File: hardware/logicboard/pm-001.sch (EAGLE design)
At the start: 16 parts, among them K1 G5V1, T1 2SC1815

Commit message: FTDI.
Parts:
- added FTDI: (no value), pinhead:PINHD-1X6
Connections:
- new net N$12: FTDI.2, U$1.GND4
- new net N$13: FTDI.3, U$1.VCC1
- new net N$14: FTDI.4, U$1.RX1-1
- new net N$15: FTDI.5, U$1.TX0-1
- new net N$16: FTDI.6, U$1.DTR
- new net N$9: FTDI.1, U$1.GND3
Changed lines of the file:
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@@
 <setting verticaltext="up"/>
 </settings>
-<grid distance="0.1" unitdist="inch" unit="inch" style="dots" multiple="1" display="yes" altdistance="0.01" altunitdist="inch" altunit="inch"/>
+<grid distance="0.1" unitdist="inch" unit="inch" style="lines" multiple="1" display="no" altdistance="0.01" altunitdist="inch" altunit="inch"/>
 <layers>
 <layer number="1" name="Top" color="4" fill="1" visible="no" active="no"/>
@@
 <part name="FRONT" library="SparkFun-Connectors" library_urn="urn:adsk.eagle:library:513" deviceset="CONN_04" device="JST-PTH" package3d_urn="urn:adsk.eagle:package:38101/1"/>
 <part name="PWR12V" library="SparkFun-Connectors" deviceset="CONN_02" device="JST-PTH-2" value="12V"/>
+<part name="FTDI" library="pinhead" library_urn="urn:adsk.eagle:library:325" deviceset="PINHD-1X6" device="" package3d_urn="urn:adsk.eagle:package:22472/2"/>
 </parts>
 <sheets>
@@
 <instance part="FRONT" gate="G$1" x="5.08" y="76.2" rot="MR180"/>
 <instance part="PWR12V" gate="G$1" x="2.54" y="35.56" rot="MR180"/>
+<instance part="FTDI" gate="A" x="76.2" y="12.7" rot="R270"/>
 </instances>
 <busses>
@@
 </segment>
 </net>
+<net name="N$9" class="0">
+<segment>
+<pinref part="U$1" gate="G$1" pin="GND3"/>
+<pinref part="FTDI" gate="A" pin="1"/>
+<wire x1="83.82" y1="15.24" x2="83.82" y2="22.86" width="0.1524" layer="91"/>
+</segment>
+</net>
+<net name="N$12" class="0">
+<segment>
+<pinref part="U$1" gate="G$1" pin="GND4"/>
+<pinref part="FTDI" gate="A" pin="2"/>
+<wire x1="81.28" y1="15.24" x2="81.28" y2="22.86" width="0.1524" layer="91"/>
+</segment>
+</net>
+<net name="N$13" class="0">
+<segment>
+<pinref part="U$1" gate="G$1" pin="VCC1"/>
+<pinref part="FTDI" gate="A" pin="3"/>
+<wire x1="78.74" y1="15.24" x2="78.74" y2="22.86" width="0.1524" layer="91"/>
+</segment>
+</net>
+<net name="N$14" class="0">
+<segment>
+<pinref part="U$1" gate="G$1" pin="RX1-1"/>
+<pinref part="FTDI" gate="A" pin="4"/>
+<wire x1="76.2" y1="15.24" x2="76.2" y2="22.86" width="0.1524" layer="91"/>
+</segment>
+</net>
+<net name="N$15" class="0">
+<segment>
+<pinref part="U$1" gate="G$1" pin="TX0-1"/>
+<pinref part="FTDI" gate="A" pin="5"/>
+<wire x1="73.66" y1="15.24" x2="73.66" y2="22.86" width="0.1524" layer="91"/>
+</segment>
+</net>
+<net name="N$16" class="0">
+<segment>
+<pinref part="U$1" gate="G$1" pin="DTR"/>
+<pinref part="FTDI" gate="A" pin="6"/>
+<wire x1="71.12" y1="15.24" x2="71.12" y2="22.86" width="0.1524" layer="91"/>
+</segment>
+</net>

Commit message: D8 -> D2.
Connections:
- net N$7: now also U$1.D2; no longer U$1.D8
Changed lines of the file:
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@@
-</segment>
-</net>
-<net name="N$7" class="0">
-<segment>
-<pinref part="R2" gate="G$1" pin="1"/>
-<pinref part="U$1" gate="G$1" pin="D8"/>
-<wire x1="106.68" y1="60.96" x2="99.06" y2="60.96" width="0.1524" layer="91"/>
 </segment>
 </net>
@@
 </segment>
 </net>
+<net name="N$7" class="0">
+<segment>
+<pinref part="R2" gate="G$1" pin="1"/>
+<wire x1="106.68" y1="60.96" x2="104.14" y2="60.96" width="0.1524" layer="91"/>
+<wire x1="104.14" y1="60.96" x2="104.14" y2="45.72" width="0.1524" layer="91"/>
+<pinref part="U$1" gate="G$1" pin="D2"/>
+<wire x1="104.14" y1="45.72" x2="99.06" y2="45.72" width="0.1524" layer="91"/>
+</segment>
+</net>

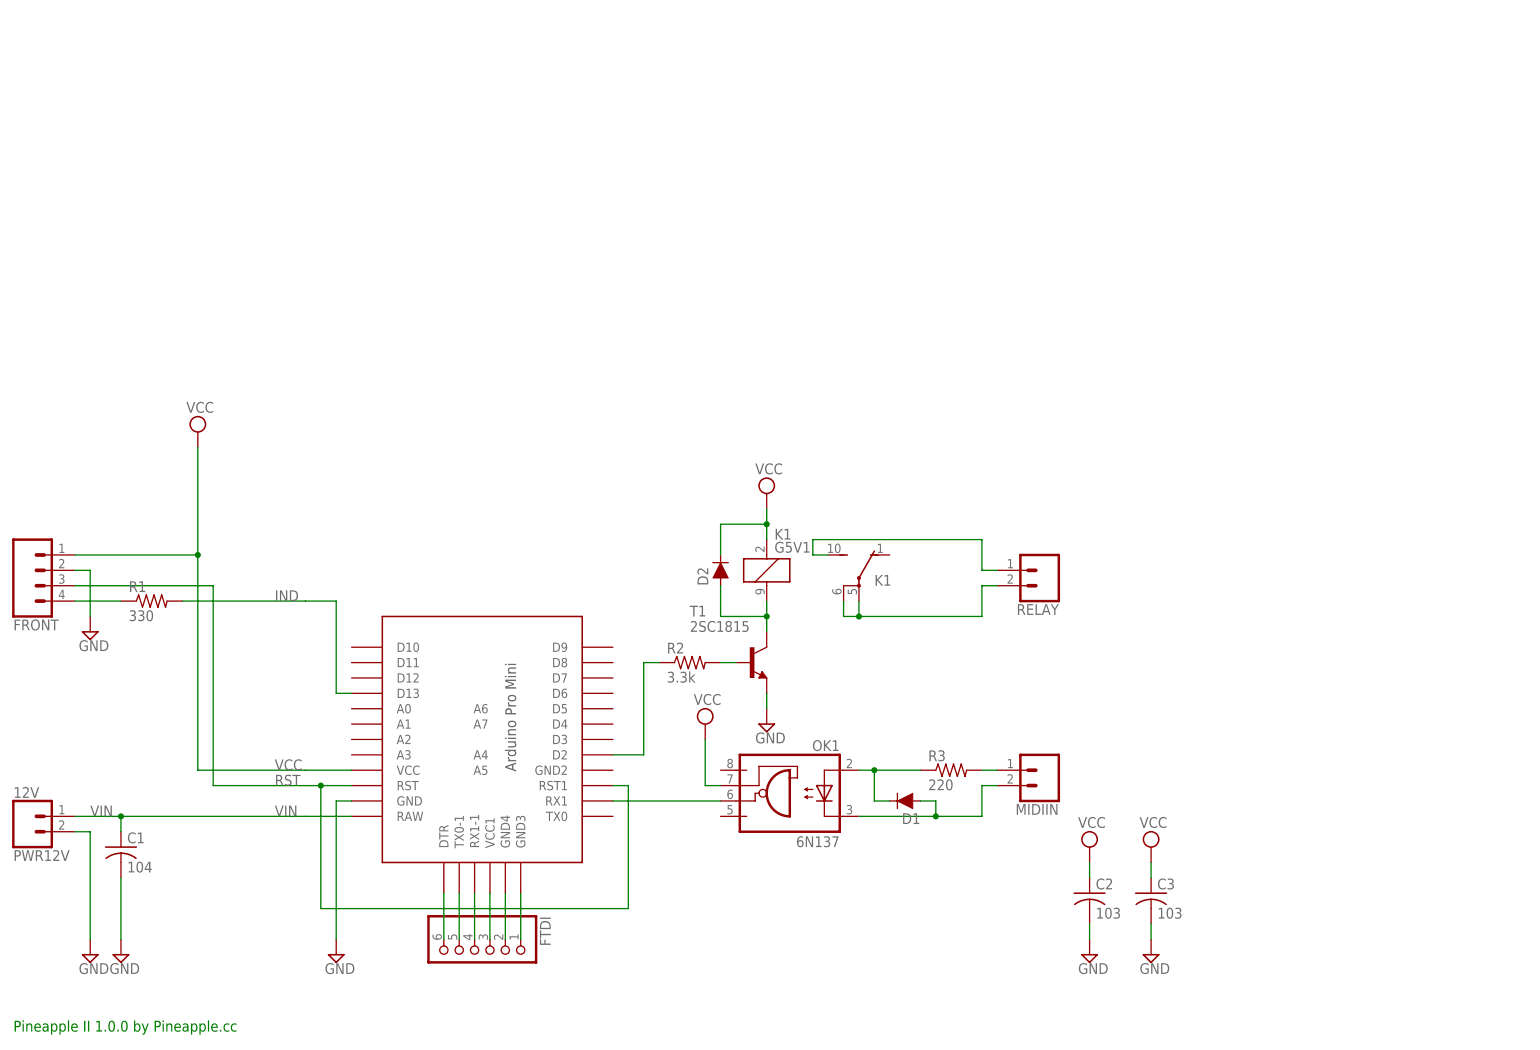
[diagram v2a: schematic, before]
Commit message: Sockets for stacking.
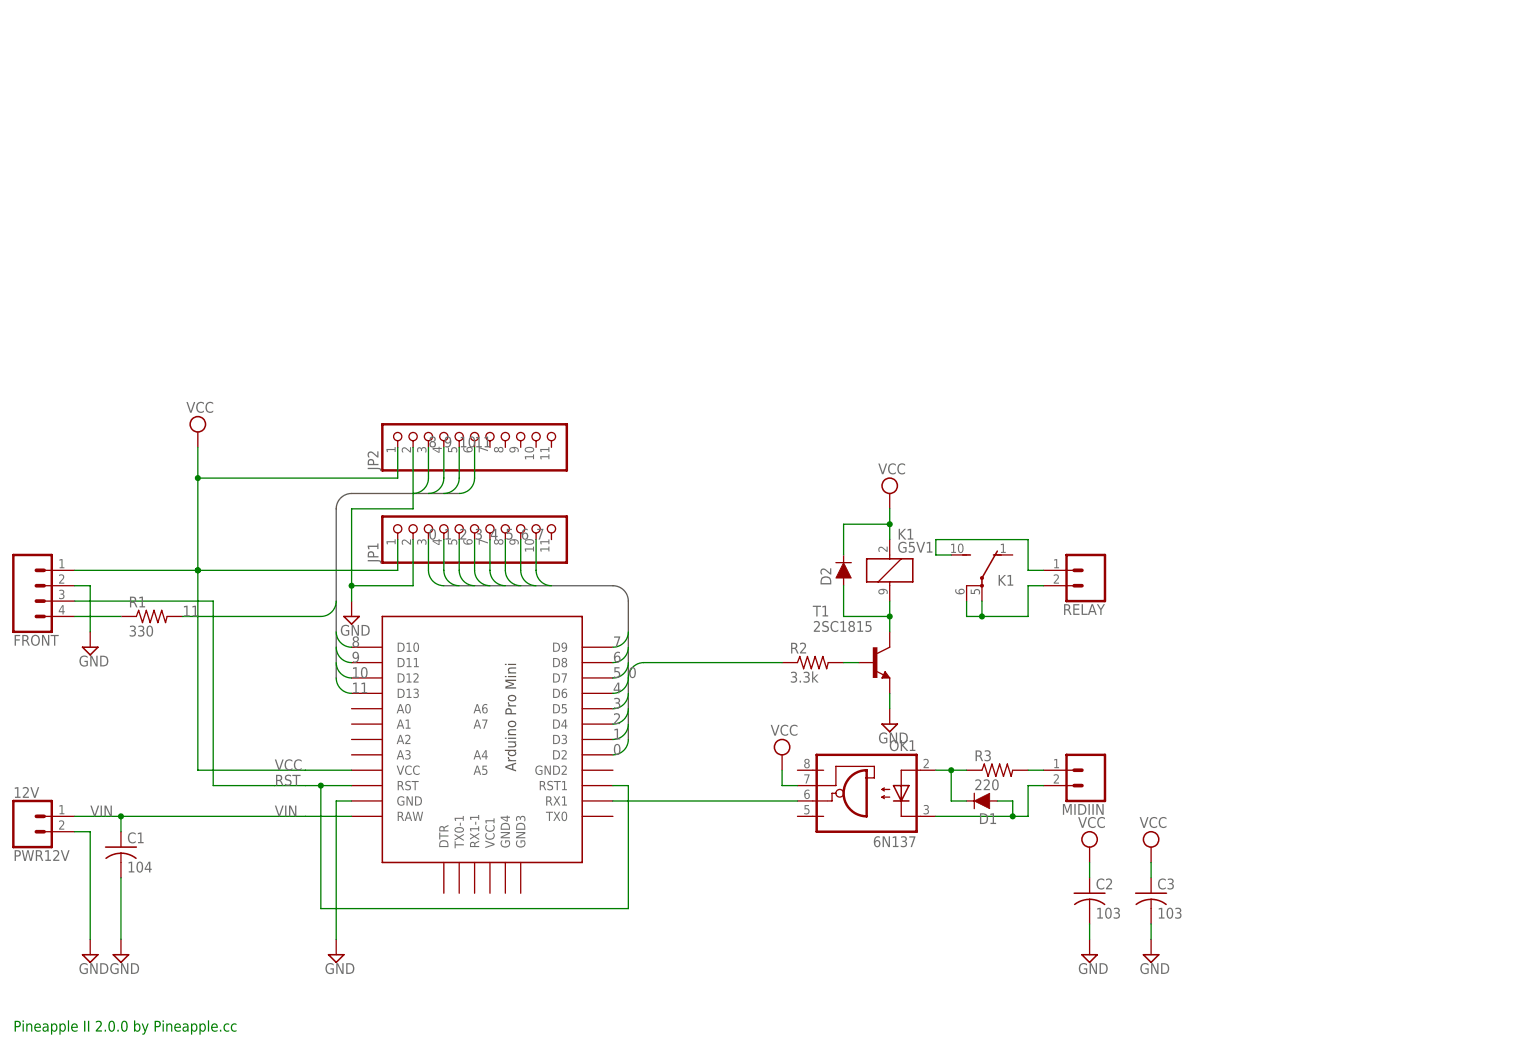
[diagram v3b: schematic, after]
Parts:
- removed FTDI: (no value), pinhead:PINHD-1X6
- added JP1, JP2: (no value), pinhead:PINHD-1X11
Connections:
- removed net IND: R1.2, U$1.D13
- removed net N$12: FTDI.2, U$1.GND4
- removed net N$13: FTDI.3, U$1.VCC1
- removed net N$14: FTDI.4, U$1.RX1-1
- removed net N$15: FTDI.5, U$1.TX0-1
- removed net N$16: FTDI.6, U$1.DTR
- removed net N$7: R2.1, U$1.D2
- removed net N$9: FTDI.1, U$1.GND3
- new net 0: JP1.3, R2.1, U$1.D2
- new net 1: JP1.4, U$1.D3
- new net 10: JP2.5, U$1.D12
- new net 11: JP2.6, R1.2, U$1.D13
- new net 2: JP1.5, U$1.D4
- new net 3: JP1.6, U$1.D5
- new net 4: JP1.7, U$1.D6
- new net 5: JP1.8, U$1.D7
- new net 6: JP1.9, U$1.D8
- new net 7: JP1.10, U$1.D9
- new net 8: JP2.3, U$1.D10
- new net 9: JP2.4, U$1.D11
- net GND: now also JP1.2, JP2.2
- net VCC: now also JP1.1, JP2.1
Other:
- note added: "Pineapple II 2.0.0 by Pineapple.cc"
- note removed: "Pineapple II 1.0.0 by Pineapple.cc"
- moved on the sheet: D1, D2, FRONT, K1, MIDIIN, OK1, R1, R2, R3, RELAY, T1

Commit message: OSHW logo.
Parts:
- added LOGO1: OSHW-LOGOL-COPPER, SparkFun-Aesthetics:OSHW-LOGOL-COPPER
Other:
- note added: "Pineapple Mini 2.0.0"
- note removed: "Pineapple II 2.0.0 by Pineapple.cc"
- moved on the sheet: C1, C2, C3, D1, D2, FRONT, JP1, JP2, K1, MIDIIN, OK1, PWR12V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

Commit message: Pineapple logo v2.
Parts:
- added U$2: PINEAPPLELOGO2, pineapplelogo2:PINEAPPLELOGO2
- LOGO1: value OSHW-LOGOL-COPPER -> OSHW-LOGOS-COPPER; device SparkFun-Aesthetics:OSHW-LOGOL-COPPER -> SparkFun-Aesthetics:OSHW-LOGOS-COPPER
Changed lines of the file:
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@@
 <part name="SUPPLY8" library="supply2" deviceset="GND" device=""/>
 <part name="FRAME1" library="frames" library_urn="urn:adsk.eagle:library:229" deviceset="A4L-LOC" device=""/>
-<part name="LOGO1" library="SparkFun-Aesthetics" deviceset="OSHW-LOGO" device="L-COPPER"/>
+<part name="U$2" library="pineapplelogo2" deviceset="PINEAPPLELOGO2" device=""/>
+<part name="LOGO1" library="SparkFun-Aesthetics" deviceset="OSHW-LOGO" device="S-COPPER"/>
 </parts>
 <sheets>
@@
 <instance part="SUPPLY8" gate="GND" x="96.52" y="88.9"/>
 <instance part="FRAME1" gate="G$1" x="0" y="0"/>
-<instance part="LOGO1" gate="G$1" x="200.66" y="15.24"/>
+<instance part="U$2" gate="G$1" x="187.96" y="7.62"/>
+<instance part="LOGO1" gate="G$1" x="238.76" y="162.56"/>
 </instances>
 <busses>

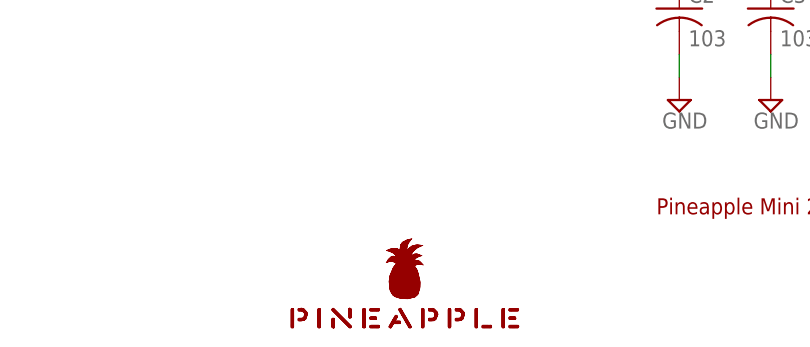
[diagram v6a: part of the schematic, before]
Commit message: New pineapple logo.
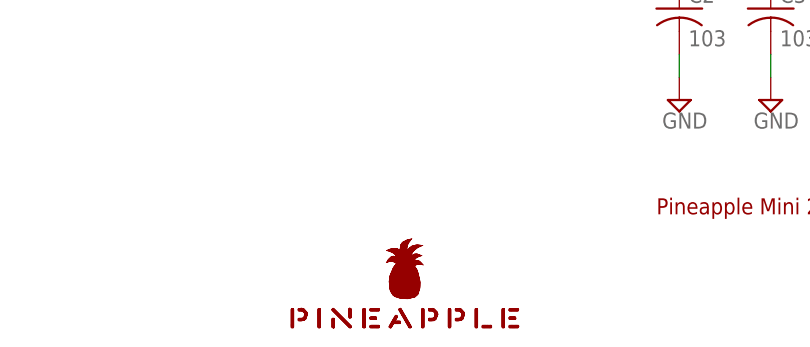
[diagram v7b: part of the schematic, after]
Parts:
- LOGO1: value OSHW-LOGOS-COPPER -> OSHW-LOGOS; device SparkFun-Aesthetics:OSHW-LOGOS-COPPER -> SparkFun-Aesthetics:OSHW-LOGOS
- U$2: value PINEAPPLELOGO2 -> PINEAPPLELOGO2SILKMINI; device pineapplelogo2:PINEAPPLELOGO2 -> pineapplelogo:PINEAPPLELOGO2SILKMINI
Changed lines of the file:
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@@
 <part name="SUPPLY8" library="supply2" deviceset="GND" device=""/>
 <part name="FRAME1" library="frames" library_urn="urn:adsk.eagle:library:229" deviceset="A4L-LOC" device=""/>
-<part name="U$2" library="pineapplelogo2" deviceset="PINEAPPLELOGO2" device=""/>
-<part name="LOGO1" library="SparkFun-Aesthetics" deviceset="OSHW-LOGO" device="S-COPPER"/>
+<part name="U$2" library="pineapplelogo" deviceset="PINEAPPLELOGO2SILKMINI" device=""/>
+<part name="LOGO1" library="SparkFun-Aesthetics" deviceset="OSHW-LOGO" device="S" value="OSHW-LOGOS"/>
 </parts>
 <sheets>

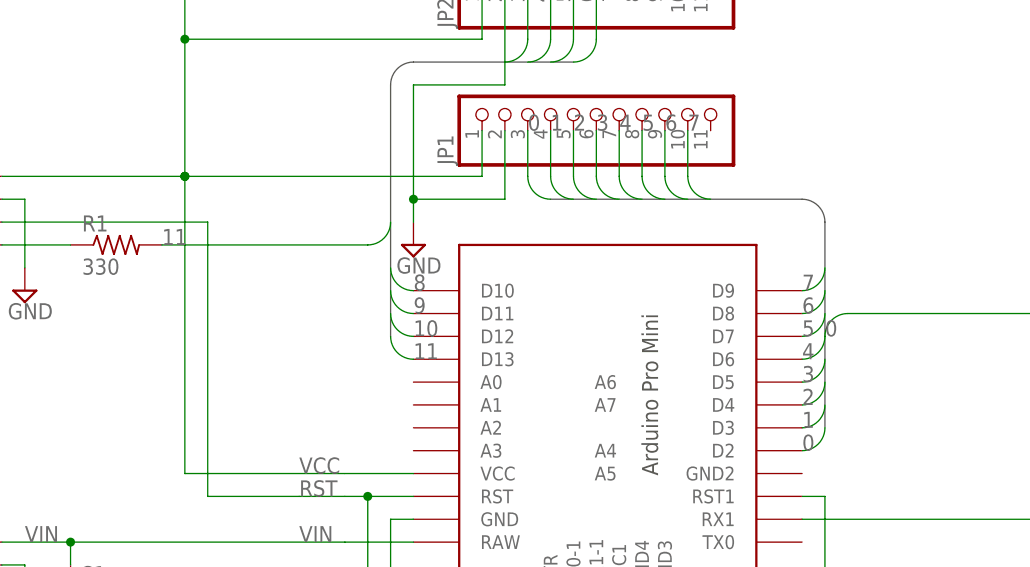
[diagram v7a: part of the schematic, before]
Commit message: Updated silk patterns and signal names.
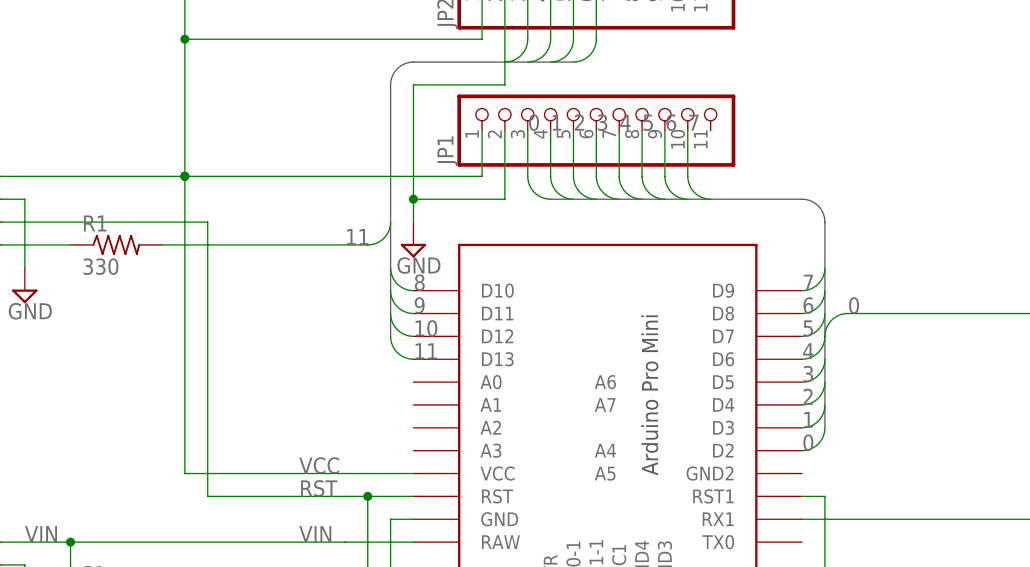
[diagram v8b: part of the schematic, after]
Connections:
- net N$1 renamed INDR
- net N$10 renamed RELAYB
- net N$11 renamed RELAYA
- net N$2 renamed MIDIIN+
- net N$3 renamed MIDIIN
- net N$5 renamed MIDIIN-
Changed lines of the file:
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@@
 </segment>
 </net>
-<net name="N$1" class="0">
+<net name="INDR" class="0">
 <segment>
 <pinref part="R1" gate="G$1" pin="1"/>
@@
 </segment>
 </net>
-<net name="N$2" class="0">
+<net name="MIDIIN+" class="0">
 <segment>
 <pinref part="R3" gate="G$1" pin="2"/>
@@
 </segment>
 </net>
-<net name="N$5" class="0">
+<net name="MIDIIN-" class="0">
 <segment>
 <pinref part="OK1" gate="A" pin="C"/>
@@
 </segment>
 </net>
-<net name="N$10" class="0">
+<net name="RELAYB" class="0">
 <segment>
 <pinref part="K1" gate="2" pin="P@1"/>
@@
 </segment>
 </net>
-<net name="N$11" class="0">
+<net name="RELAYA" class="0">
 <segment>
 <pinref part="K1" gate="2" pin="S"/>
@@
 </segment>
 </net>
-<net name="N$3" class="0">
+<net name="MIDIIN" class="0">
 <segment>
 <pinref part="OK1" gate="A" pin="VO"/>
@@
 <wire x1="167.64" y1="81.28" x2="144.78" y2="81.28" width="0.1524" layer="91"/>
 <wire x1="144.78" y1="81.28" x2="142.24" y2="78.74" width="0.1524" layer="91" curve="90"/>
-<label x="142.24" y="78.74" size="1.778" layer="95"/>
+<label x="144.78" y="81.28" size="1.778" layer="95"/>
 </segment>
 </net>
@@
 <wire x1="93.98" y1="91.44" x2="91.44" y2="88.9" width="0.1524" layer="91" curve="-90"/>
 <wire x1="91.44" y1="88.9" x2="68.58" y2="88.9" width="0.1524" layer="91"/>
-<label x="68.58" y="88.9" size="1.778" layer="95"/>
-</segment>
-</net>
+<label x="88.9" y="88.9" size="1.778" layer="95"/>
+</segment>
+</net>
